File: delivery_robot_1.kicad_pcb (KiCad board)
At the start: 4 copper layers, 100 x 106 mm, 179 parts, among them J1 SWD, J13 Pi 5 link, J14 Pi 5 power, J15 Motor2 encoder, J16 MDD20A PWM2/DIR2/GND, J17 Latch servo, J18 AUX1 Notecard, J19 AUX2 LiDAR, J2 XT30PW-M, J20 AUX3 GNSS, J21 AUX4 IMU, J22 AUX force-on, J23 SHUNT SENSE: LOAD / BATT, J24 INTERIOR LIGHT, J4 BOOT0 jumper, J5 Power test points, J6 MDD20A PWM1/DIR1/GND, J7 Motor1 encoder, J8 Expansion header, Q1 SQJ409EP, Q2 DMN63D8L, SW1 RESET, U1 STM32F091RCTx, U10 74LVC2G17, U11 USBLC6-2SC6, U12 USBLC6-2SC6, U13 INA228AIDGSR, U14 SN74LV1T125DBVR, U2 TPS56637RPAR, U3 TPS54202HDDCR, U4 TPS7A8101DRBR, U5 TPS56637RPAR, U6 USBLC6-2SC6, U7 USBLC6-2SC6, U8 SN74LVC1T45DBV, U9 74LVC2G17, Y3 8MHz

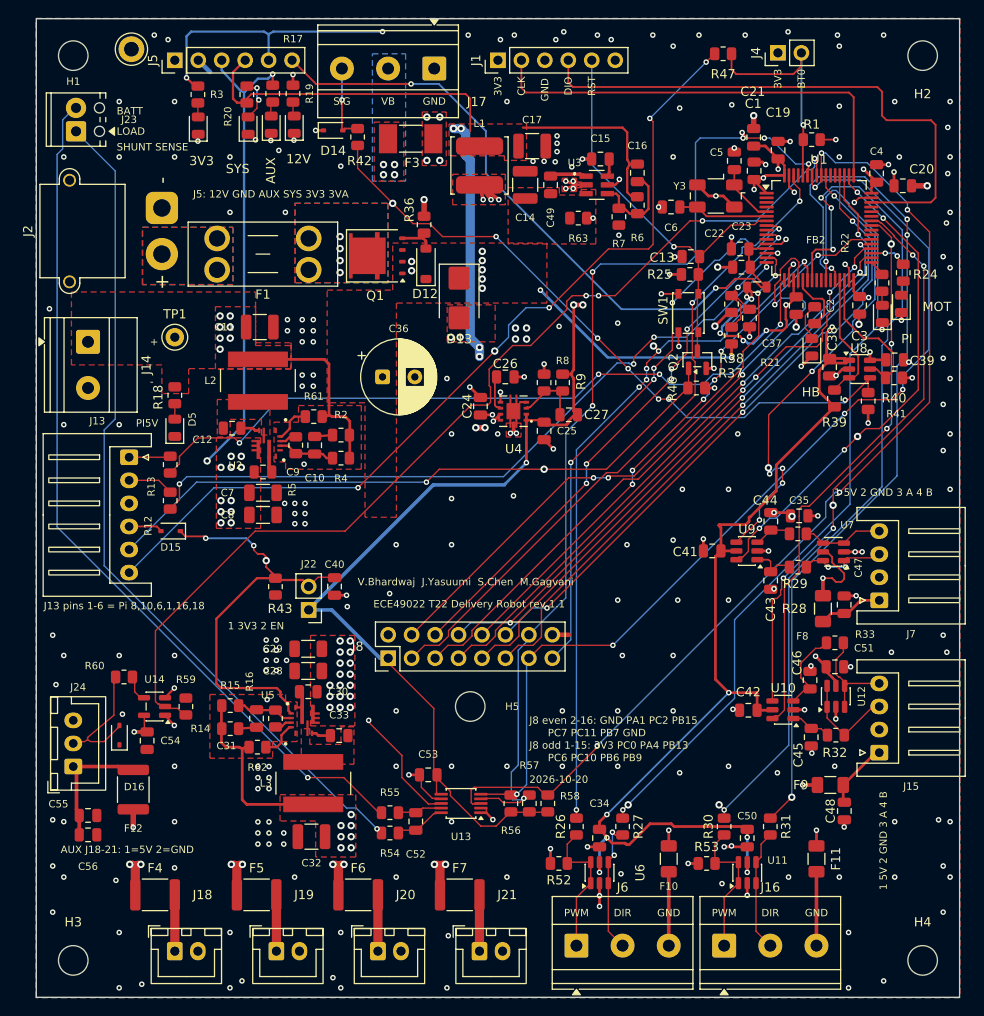
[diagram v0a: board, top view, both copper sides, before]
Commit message: Enlarge vias to 15.7 mil holes for flywiring
All vias now have a 0.4 mm (15.7 mil) drill, above the 15 mil minimum
needed to solder 28 AWG rework wire. Former 0.3/0.6 mm vias are
0.4/0.66 mm (0.13 mm annular ring). Vias that no longer fit were
nudged, and 17 signal nets around U1 and J8 were rerouted. The
netclass via sizes, via preset and DRC minimums are raised to match
so new vias cannot be undersized.

DRC: 0 violations, 0 unconnected, 0 parity issues.
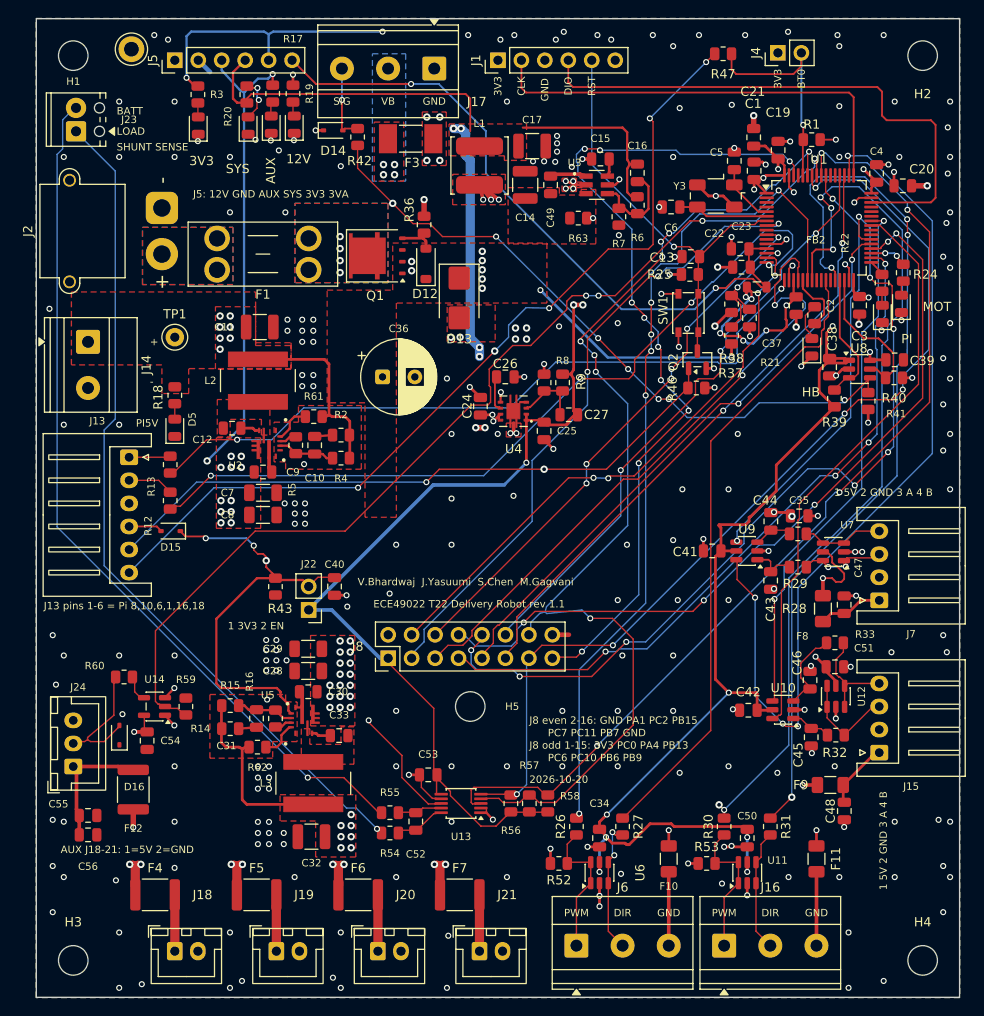
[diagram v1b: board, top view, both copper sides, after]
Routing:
- net ENC1_A: track 54.4 -> 96.6 mm, vias 5 -> 4
- net PC7: track 62.7 -> 93.3 mm, vias 6 -> 8
- net PB9: track 65.9 -> 92.8 mm, vias 5 -> 10
- net MOTOR1_DIR: track 92.5 -> 68.6 mm, vias 3 -> 0
- net PB15: track 65.3 -> 85.0 mm
- net MOTOR1_PWM: track 77.4 -> 92.6 mm, vias 7 -> 6
- net PB13: track 63.7 -> 77.1 mm, vias 2 -> 4
- net PB7: track 107.7 -> 116.7 mm, vias 7 -> 8
- net USART2_TX: track 77.5 -> 86.1 mm
- net ENC1_B: track 51.1 -> 46.7 mm, vias 7 -> 2
- net PC11: track 69.3 -> 65.7 mm
- net ENC2_B: track 61.8 -> 58.3 mm, vias 5 -> 2
- net PC10: track 70.6 -> 67.4 mm
- net USART2_RX: track 79.7 -> 77.6 mm, vias 4 -> 2
- net ENC2_A: track 60.9 -> 62.9 mm, vias 3 -> 0
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
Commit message: Swap U13 to INA237 and set the Pi rail to 5.10 V
U13: INA228AIDGSR -> INA237AIDGSR. The INA228 is out of stock at TI,
LCSC and Mouser (next Mouser stock May 2027), and the INA238 is out
too. The INA237 has the same VSSOP-10 pinout, -0.3 V to 85 V common
mode, 0x40 address and +/-163.84 mV range, and Mouser stocks it. U13
keeps the Sensor_Energy:INA228 symbol (identical pins); only Value,
MPN, Datasheet and Description change, in the schematic and on the
board. It is 16-bit and has no CHARGE register, so firmware now
integrates current; the design-change doc has the new SHUNT_CAL
(819.2e6 x 4 mA x 1.5 mOhm = 4915) and accuracy budget.

R4: 73.2k -> 75k (RC0805FR-0775KL). +5V_PI = 0.6 V x (1 + 75/10) =
5.10 V instead of 4.99 V, back to the original design's ~5.1 V target
for harness drop at 5 A. R15 (AUX) stays 73.2k.

No connectivity, footprint or copper changes. delivery_robot_1.pdf,
system-ERC-report.txt and system-netlist.xml regenerated with KiCad
10.0.6 (the saved netlist was still from before the buck swap).

ERC: 0 errors, 0 warnings. DRC: 0 violations (4 excluded test vias),
0 unconnected, 0 parity issues.
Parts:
- R4: value 73.2k -> 75k
- U13: value INA228AIDGSR -> INA237AIDGSR
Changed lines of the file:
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@@
 			)
 		)
-		(property "Description" "INA228 IN+ series filter / dV/dt protection (TI SLYS021A 8.1.4). Place at U13."
+		(property "Description" "INA237 IN+ series filter / dV/dt protection (TI SBOSA20A). Place at U13."
 			(at 0 0 0)
 			(layer "F.Fab")
@@
 			)
 		)
-		(property "Value" "73.2k"
+		(property "Value" "75k"
 			(at 0 1.65 180)
 			(layer "F.Fab")
@@
 			)
 		)
-		(property "MPN" "RC0805FR-0773K2L"
+		(property "MPN" "RC0805FR-0775KL"
 			(at 0 0 180)
 			(layer "F.SilkS")
@@
 			)
 		)
-		(property "Specification" "73.2k 1% (Rfbt)"
+		(property "Specification" "75k 1% (Rfbt), sets +5V_PI to 5.10 V"
 			(at 0 0 180)
 			(layer "F.SilkS")
@@
 			)
 		)
-		(property "Description" "Differential filter across INA228 IN+/IN- (with R54/R55, about 80 kHz). No ground connection."
+		(property "Description" "Differential filter across INA237 IN+/IN- (with R54/R55, about 80 kHz). No ground connection."
 			(at 0 0 90)
 			(layer "F.Fab")
@@
 			)
 		)
-		(property "Description" "INA228 IN- series filter / dV/dt protection (TI SLYS021A 8.1.4). Place at U13."
+		(property "Description" "INA237 IN- series filter / dV/dt protection (TI SBOSA20A). Place at U13."
 			(at 0 0 0)
 			(layer "F.Fab")
@@
 			)
 		)
-		(property "Description" "INA228 ALERT pull-up (open-drain, active low) on BATT_ALERT / PB4."
+		(property "Description" "INA237 ALERT pull-up (open-drain, active low) on BATT_ALERT / PB4."
 			(at 0 0 90)
 			(layer "F.Fab")
@@
 			)
 		)
-		(property "Value" "INA228AIDGSR"
+		(property "Value" "INA237AIDGSR"
 			(at 0 2.45 180)
 			(layer "F.Fab")
@@
 			)
 		)
-		(property "Datasheet" "https://www.ti.com/lit/ds/symlink/ina228.pdf"
+		(property "Datasheet" "https://www.ti.com/lit/ds/symlink/ina237.pdf"
 			(at 0 0 180)
 			(layer "F.Fab")
@@
 			)
 		)
-		(property "Description" "20-bit power/energy/charge monitor, I2C, 85 V, -0.3 V common mode. Low-side on the off-board battery shunt; address 0x40. DGS (VSSOP-10) package; KiCad TSSOP-10_3x3mm_P0.5mm is the TI DGS outline."
+		(property "Description" "16-bit current/voltage/power monitor, I2C, 85 V, -0.3 V common mode (same pinout as INA228; uses the INA228 symbol). Low-side on the off-board battery shunt; address 0x40. Charge is integrated in firmware. DGS (VSSOP-10) package; KiCad TSSOP-10_3x3mm_P0.5mm is the TI DGS outline."
 			(at 0 0 180)
 			(layer "F.Fab")
@@
 			)
 		)
-		(property "MPN" "INA228AIDGSR"
+		(property "MPN" "INA237AIDGSR"
 			(at 0 0 180)
 			(layer "F.SilkS")

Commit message: Apply TA layout review: vias off pads, obtuse corners, buck layouts
- Move every via off its pad. The +3V3 vias at U6/U11/C34/C50 sit
  0.03-0.06 mm from the pad edge, without overlap, and are tented.
- Remove the remaining acute and right-angle track corners, including
  where tracks leave a pad, and straighten small jogs (R27 pin 2).
- U2/U5: add a second 47 uF output cap (C57, C58) to match the
  two-Cout datasheet layout, and add more PGND vias. F1 moves up 1 mm
  to make room for C57.
- U3: move C14 down 1 mm so the input cap GND pads have a via on each
  side.

DRC: 0 violations, 0 unconnected, 0 parity issues. ERC clean.
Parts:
- added C57: 47uF, Capacitor_SMD:C_1210_3225Metric, F.Cu at (109.2, 80.1)
- added C58: 47uF, Capacitor_SMD:C_1210_3225Metric, F.Cu at (114.3, 141.9)
- moved C14 1.00 mm to (137.9, 69.0)
- moved F1 1.00 mm to (114.5, 76.2)
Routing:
- net GND: track 103.5 -> 127.3 mm, vias 264 -> 280
- net USART2_TX: track 86.1 -> 77.1 mm
- net /Motor Control/ENC1_A_CONN: track 9.80 -> 15.8 mm
- net VBAT_SENSE: track 15.1 -> 17.1 mm
- net PB7: track 116.7 -> 118.0 mm
- net /Buck 5V SYS/FB: track 10.2 -> 11.2 mm
- net +3V3: track 280.3 -> 281.2 mm, vias 25 -> 24
- net BATT_ALERT: track 107.8 -> 108.7 mm
- net /Battery Monitor/INA_INP: track 5.46 -> 4.76 mm
- net /Motor Control/MOTOR1_DIR_CONN: track 14.5 -> 13.9 mm
- net +5V_AUX: track 87.4 -> 86.9 mm
- net /Buck 5V SYS/EN: track 8.87 -> 9.42 mm
- net /Motor Control/ENC2_B_F: track 9.23 -> 8.71 mm
- net PB6: track 105.3 -> 104.8 mm
- net PB13: track 77.1 -> 77.6 mm
